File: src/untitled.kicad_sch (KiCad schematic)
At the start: 47 parts, among them J5 USB_C_Receptacle_USB2.0_14P, J6 Conn_02x26_Odd_Even, J7 SM03B-SRSS-TB, J8 Conn_02x26_Odd_Even, U4 W25Q128JVS, U5 NCP1117-1.5_SOT223, Y2 ABM8-272-T3

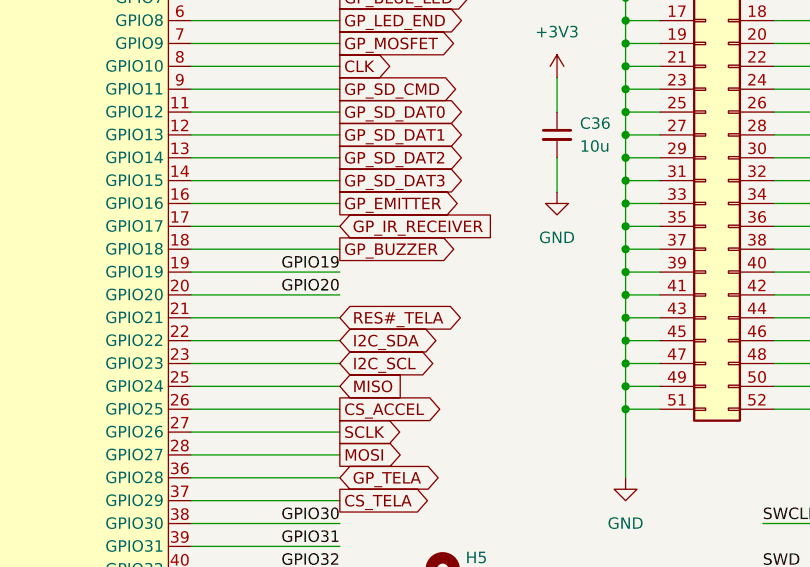
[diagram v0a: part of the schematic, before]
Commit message: fix: Consertando paginação e refact da Tela_OLED
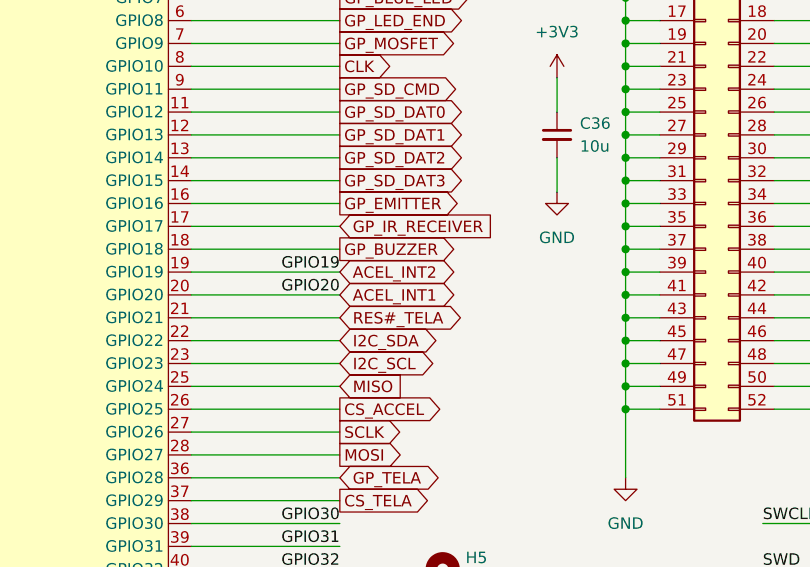
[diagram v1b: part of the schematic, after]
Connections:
- net GPIO19 renamed ACEL_INT2
- net GPIO20 renamed ACEL_INT1
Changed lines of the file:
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@@
+		)
+	)
+	(global_label "ACEL_INT1"
+		(shape bidirectional)
+		(at 179.07 114.3 0)
+		(fields_autoplaced yes)
+		(effects
+			(font
+				(size 1.27 1.27)
+			)
+			(justify left)
+		)
+		(property "Intersheetrefs" "${INTERSHEET_REFS}"
+			(at 192.7822 114.3 0)
+			(effects
+				(font
+					(size 1.27 1.27)
+				)
+				(justify left)
+				(hide yes)
+			)
 		)
 	)
@@
 			(effects
 				(font
+					(size 1.27 1.27)
+				)
+				(justify left)
+				(hide yes)
+			)
+		)
+	)
+	(global_label "ACEL_INT2"
+		(shape bidirectional)
+		(at 179.07 111.76 0)
+		(fields_autoplaced yes)
+		(effects
+			(font
+				(size 1.27 1.27)
+			)
+			(justify left)
+		)
+		(property "Intersheetrefs" "${INTERSHEET_REFS}"
+			(at 192.7822 111.76 0)
+			(effects
+				(font

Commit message: revisão da RP2040
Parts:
- removed J7: SM03B-SRSS-TB, Connector_JST:JST_SH_SM03B-SRSS-TB_1x03-1MP_P1.00mm_Horizontal, symbol Connector_Generic_MountingPin:Conn_01x03_MountingPin
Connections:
- net GPIO32 renamed UART0 TX
- net GPIO33 renamed UART0 RX
- net SWD renamed SWDIO
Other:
- moved on the sheet: H5, H6, H7, H8

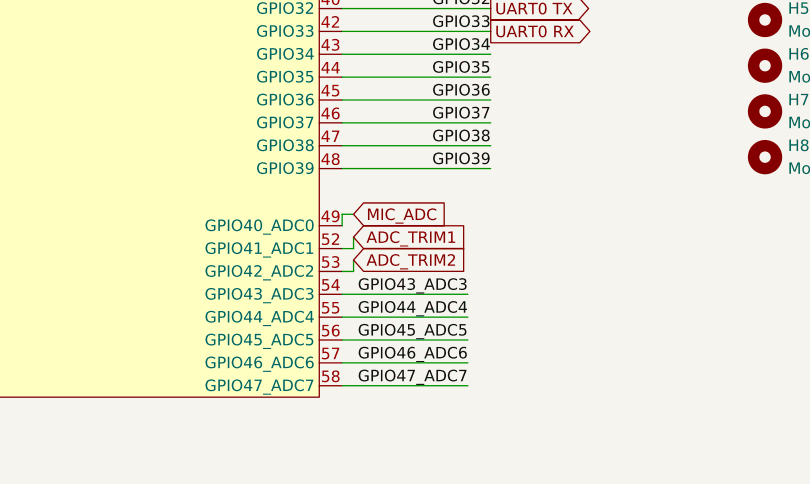
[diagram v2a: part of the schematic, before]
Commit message: LDR adicionado
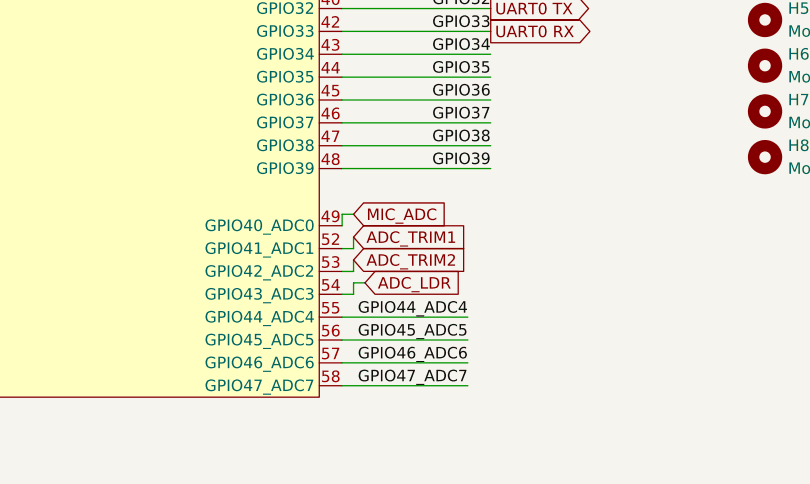
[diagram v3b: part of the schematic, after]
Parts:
- J5: footprint (none) -> Connector_USB:USB_C_Receptacle_GCT_USB4105-xx-A_16P_TopMnt_Horizontal
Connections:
- net GPIO43_ADC3: no longer U6.54 (GPIO43_ADC3)
- new net ADC_LDR: U6.54 (GPIO43_ADC3)
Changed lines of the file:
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@@
 	(wire
 		(pts
-			(xy 162.56 176.53) (xy 176.53 176.53)
+			(xy 163.83 175.26) (xy 165.1 175.26)
 		)
 		(stroke
@@
 	(wire
 		(pts
+			(xy 163.83 176.53) (xy 162.56 176.53)
+		)
+		(stroke
+			(width 0)
+			(type default)
+		)
+	)
+	(wire
+		(pts
 			(xy 238.76 121.92) (xy 227.33 121.92)
 		)
@@
 	(wire
 		(pts
+			(xy 163.83 175.26) (xy 163.83 176.53)
+		)
+		(stroke
+			(width 0)
+			(type default)
+		)
+	)
+	(wire
+		(pts
 			(xy 27.94 119.38) (xy 39.37 119.38)
 		)
@@
 		)
 	)
-	(label "GPIO43_ADC3"
-		(at 176.53 176.53 180)
-		(effects
-			(font
-				(size 1.27 1.27)
-			)
-			(justify right bottom)
-		)
-	)
 	(label "GPIO40_ADC0"
 		(at 241.3 81.28 0)
@@
 		)
 	)
+	(global_label "ADC_LDR"
+		(shape input)
+		(at 165.1 175.26 0)
+		(fields_autoplaced yes)
+		(effects
+			(font
+				(size 1.27 1.27)
+			)
+			(justify left)
+		)
+		(property "Intersheetrefs" "${INTERSHEET_REFS}"
+			(at 176.2495 175.26 0)
+			(effects
+				(font
+					(size 1.27 1.27)
+				)
+				(justify left)
+				(hide yes)
+			)
+		)
+	)
 	(global_label "GP_SW3"
 		(shape input)
@@
 			)
 		)
-		(property "Footprint" ""
+		(property "Footprint" "Connector_USB:USB_C_Receptacle_GCT_USB4105-xx-A_16P_TopMnt_Horizontal"
 			(at 34.29 39.37 0)
 			(effects

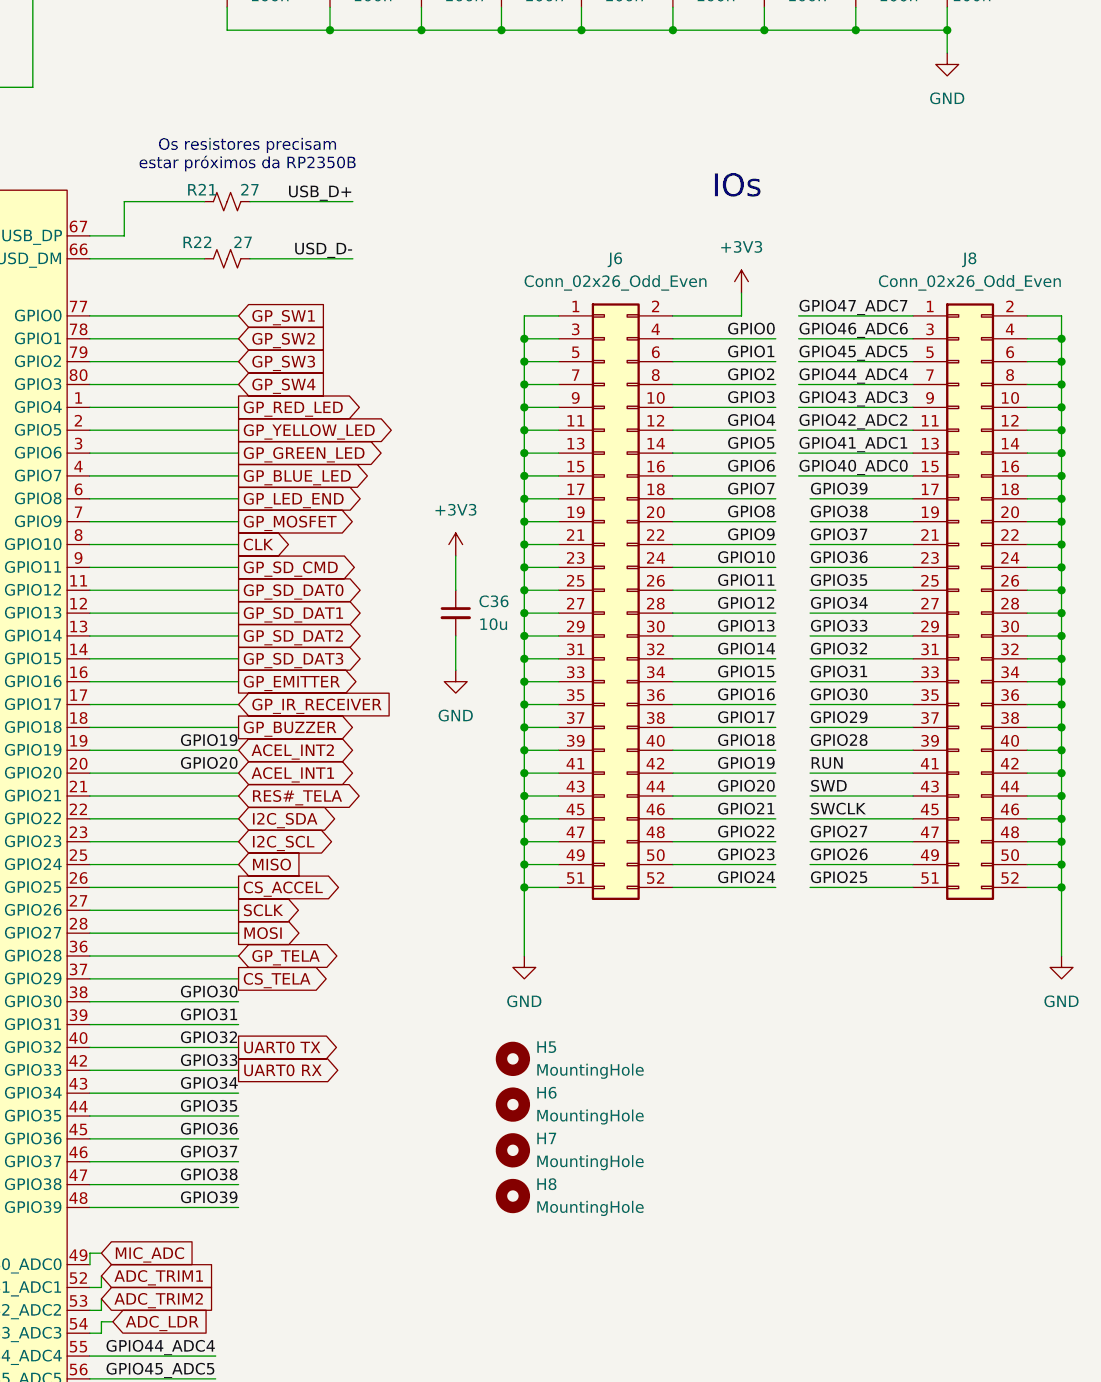
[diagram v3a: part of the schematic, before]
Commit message: footprints MCU ok
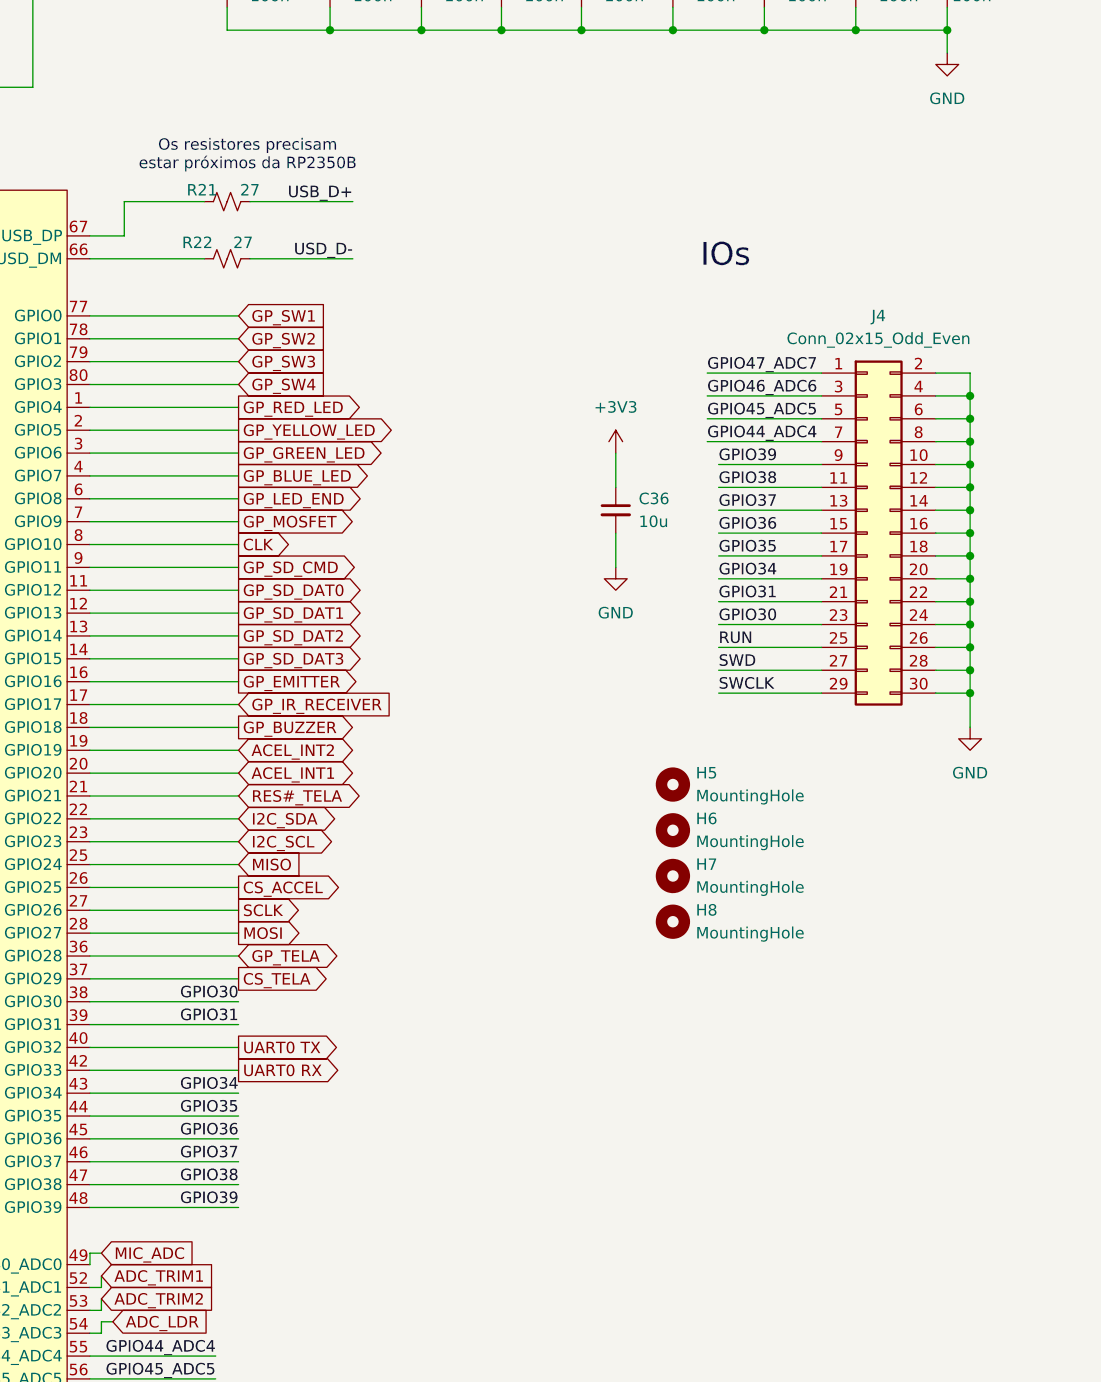
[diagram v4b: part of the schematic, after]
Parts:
- removed J6: Conn_02x26_Odd_Even, symbol Connector_Generic:Conn_02x26_Odd_Even
- removed J8: Conn_02x26_Odd_Even, Connector_PinHeader_2.54mm:PinHeader_2x26_P2.54mm_Vertical, symbol Connector_Generic:Conn_02x26_Odd_Even
- added J4: Conn_02x15_Odd_Even, Connector_PinHeader_1.00mm:PinHeader_2x15_P1.00mm_Vertical_SMD, symbol Connector_Generic:Conn_02x15_Odd_Even
- U6: footprint (none) -> componentes_personalizados:RP2350B
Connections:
- net GND: now also J4.10 (Pin_10), J4.12 (Pin_12), J4.14 (Pin_14), J4.16 (Pin_16), J4.18 (Pin_18), J4.2 (Pin_2), J4.20 (Pin_20), J4.22 (Pin_22), J4.24 (Pin_24), J4.26 (Pin_26), J4.28 (Pin_28), J4.30 (Pin_30), J4.4 (Pin_4), J4.6 (Pin_6), J4.8 (Pin_8)
- net GPIO30: now also J4.23 (Pin_23)
- net GPIO31: now also J4.21 (Pin_21)
- net GPIO34: now also J4.19 (Pin_19)
- net GPIO35: now also J4.17 (Pin_17)
- net GPIO36: now also J4.15 (Pin_15)
- net GPIO37: now also J4.13 (Pin_13)
- net GPIO38: now also J4.11 (Pin_11)
- net GPIO39: now also J4.9 (Pin_9)
- net GPIO44_ADC4: now also J4.7 (Pin_7)
- net GPIO45_ADC5: now also J4.5 (Pin_5)
- net GPIO46_ADC6: now also J4.3 (Pin_3)
- net GPIO47_ADC7: now also J4.1 (Pin_1)
- net RUN: now also J4.25 (Pin_25)
- net SWCLK: now also J4.29 (Pin_29)
- net SWDIO: now also J4.27 (Pin_27)
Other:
- moved on the sheet: C36, H5, H6, H7, H8

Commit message: Footprints adicionados GPIOS
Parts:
- SW_RUN1: footprint Button_Switch_SMD:SW_Push_1P1T_NO_CK_PTS125Sx43PSMTR -> Button_Switch_SMD:SW_Tactile_SPST_NO_Straight_CK_PTS636Sx25SMTRLFS
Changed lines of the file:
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@@
 			)
 		)
-		(property "Footprint" "Button_Switch_SMD:SW_Push_1P1T_NO_CK_PTS125Sx43PSMTR"
+		(property "Footprint" "Button_Switch_SMD:SW_Tactile_SPST_NO_Straight_CK_PTS636Sx25SMTRLFS"
 			(at 87.63 127 0)
 			(effects
